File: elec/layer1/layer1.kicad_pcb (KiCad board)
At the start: 2 copper layers, 178 x 173.3 mm, 0 parts

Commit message: chore: l1 mux routing
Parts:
- added C1: 100nF, Capacitor_SMD:C_0603_1608Metric, F.Cu at (-14.4, 33.8)
- added C2: 100nF, Capacitor_SMD:C_0603_1608Metric, F.Cu at (-14.4, 36.3)
- added C3: 1000uF, Capacitor_THT:CP_Radial_D16.0mm_P7.50mm, F.Cu at (28.8, 127.8)
- added C4: 1000uF, Capacitor_THT:CP_Radial_D16.0mm_P7.50mm, F.Cu at (46.1, 127.3)
- added D1: LED, LED_SMD:LED_PLCC_2835, B.Cu at (109.6, 55.8)
- added D10: LED, LED_SMD:LED_PLCC_2835, B.Cu at (159.6, 116.7)
- added D11: LED, LED_SMD:LED_PLCC_2835, B.Cu at (156.7, 126.3)
- added D12: LED, LED_SMD:LED_PLCC_2835, B.Cu at (152.0, 135.1)
- added D13: LED, LED_SMD:LED_PLCC_2835, B.Cu at (145.7, 142.9)
- added D14: LED, LED_SMD:LED_PLCC_2835, B.Cu at (137.9, 149.2)
- added D15: LED, LED_SMD:LED_PLCC_2835, B.Cu at (129.1, 153.9)
- added D16: LED, LED_SMD:LED_PLCC_2835, B.Cu at (119.6, 156.8)
- added D17: LED, LED_SMD:LED_PLCC_2835, B.Cu at (109.6, 157.8)
- added D18: LED, LED_SMD:LED_PLCC_2835, B.Cu at (99.7, 156.8)
- added D19: LED, LED_SMD:LED_PLCC_2835, B.Cu at (90.1, 153.9)
- added D2: LED, LED_SMD:LED_PLCC_2835, B.Cu at (119.6, 56.8)
- added D20: LED, LED_SMD:LED_PLCC_2835, B.Cu at (81.3, 149.2)
- added D21: LED, LED_SMD:LED_PLCC_2835, B.Cu at (73.5, 142.9)
- added D22: LED, LED_SMD:LED_PLCC_2835, B.Cu at (67.2, 135.1)
- added D23: LED, LED_SMD:LED_PLCC_2835, B.Cu at (62.5, 126.3)
- added D24: LED, LED_SMD:LED_PLCC_2835, B.Cu at (59.6, 116.7)
- added D25: LED, LED_SMD:LED_PLCC_2835, B.Cu at (58.6, 106.8)
- added D26: LED, LED_SMD:LED_PLCC_2835, B.Cu at (59.6, 96.8)
- added D27: LED, LED_SMD:LED_PLCC_2835, B.Cu at (62.5, 87.3)
- added D28: LED, LED_SMD:LED_PLCC_2835, B.Cu at (67.2, 78.5)
- added D29: LED, LED_SMD:LED_PLCC_2835, B.Cu at (73.5, 70.7)
- added D3: LED, LED_SMD:LED_PLCC_2835, B.Cu at (129.1, 59.7)
- added D30: LED, LED_SMD:LED_PLCC_2835, B.Cu at (81.3, 64.4)
- added D31: LED, LED_SMD:LED_PLCC_2835, B.Cu at (90.1, 59.7)
- added D32: LED, LED_SMD:LED_PLCC_2835, B.Cu at (99.7, 56.8)
- added D33: D_Photo, Diode_SMD:D_0603_1608Metric, B.Cu at (104.6, 55.5)
- added D34: D_Photo, Diode_SMD:D_0603_1608Metric, B.Cu at (94.7, 57.5)
- added D35: D_Photo, Diode_SMD:D_0603_1608Metric, B.Cu at (85.3, 61.4)
- added D36: D_Photo, Diode_SMD:D_0603_1608Metric, B.Cu at (76.9, 67.0)
- added D37: D_Photo, Diode_SMD:D_0603_1608Metric, B.Cu at (69.8, 74.1)
- added D38: D_Photo, Diode_SMD:D_0603_1608Metric, B.Cu at (64.2, 82.5)
- added D39: D_Photo, Diode_SMD:D_0603_1608Metric, B.Cu at (60.3, 91.8)
- added D4: LED, LED_SMD:LED_PLCC_2835, B.Cu at (137.9, 64.4)
- added D40: D_Photo, Diode_SMD:D_0603_1608Metric, B.Cu at (58.4, 101.7)
- added D41: D_Photo, Diode_SMD:D_0603_1608Metric, B.Cu at (58.4, 111.8)
- added D42: D_Photo, Diode_SMD:D_0603_1608Metric, B.Cu at (60.3, 121.7)
- added D43: D_Photo, Diode_SMD:D_0603_1608Metric, B.Cu at (64.2, 131.1)
- added D44: D_Photo, Diode_SMD:D_0603_1608Metric, B.Cu at (69.8, 139.5)
- added D45: D_Photo, Diode_SMD:D_0603_1608Metric, B.Cu at (76.9, 146.6)
- added D46: D_Photo, Diode_SMD:D_0603_1608Metric, B.Cu at (85.3, 152.2)
- added D47: D_Photo, Diode_SMD:D_0603_1608Metric, B.Cu at (94.7, 156.1)
- added D48: D_Photo, Diode_SMD:D_0603_1608Metric, B.Cu at (104.6, 158.0)
- added D49: D_Photo, Diode_SMD:D_0603_1608Metric, B.Cu at (114.7, 158.0)
- added D5: LED, LED_SMD:LED_PLCC_2835, B.Cu at (145.7, 70.7)
- added D50: D_Photo, Diode_SMD:D_0603_1608Metric, B.Cu at (124.6, 156.1)
- added D51: D_Photo, Diode_SMD:D_0603_1608Metric, B.Cu at (133.9, 152.2)
- added D52: D_Photo, Diode_SMD:D_0603_1608Metric, B.Cu at (142.3, 146.6)
- added D53: D_Photo, Diode_SMD:D_0603_1608Metric, B.Cu at (149.4, 139.5)
- added D54: D_Photo, Diode_SMD:D_0603_1608Metric, B.Cu at (155.0, 131.1)
- added D55: D_Photo, Diode_SMD:D_0603_1608Metric, B.Cu at (158.9, 121.7)
- added D56: D_Photo, Diode_SMD:D_0603_1608Metric, B.Cu at (160.9, 111.8)
- added D57: D_Photo, Diode_SMD:D_0603_1608Metric, B.Cu at (160.9, 101.7)
- added D58: D_Photo, Diode_SMD:D_0603_1608Metric, B.Cu at (158.9, 91.8)
- added D59: D_Photo, Diode_SMD:D_0603_1608Metric, B.Cu at (155.0, 82.5)
- added D6: LED, LED_SMD:LED_PLCC_2835, B.Cu at (152.0, 78.5)
- added D60: D_Photo, Diode_SMD:D_0603_1608Metric, B.Cu at (149.4, 74.1)
- added D61: D_Photo, Diode_SMD:D_0603_1608Metric, B.Cu at (142.3, 67.0)
- added D62: D_Photo, Diode_SMD:D_0603_1608Metric, B.Cu at (133.9, 61.4)
- added D63: D_Photo, Diode_SMD:D_0603_1608Metric, B.Cu at (124.6, 57.5)
- added D64: D_Photo, Diode_SMD:D_0603_1608Metric, B.Cu at (114.7, 55.5)
- added D7: LED, LED_SMD:LED_PLCC_2835, B.Cu at (156.7, 87.3)
- added D8: LED, LED_SMD:LED_PLCC_2835, B.Cu at (159.6, 96.8)
- added D9: LED, LED_SMD:LED_PLCC_2835, B.Cu at (160.6, 106.8)
- added H1: MountingHole, MountingHole:MountingHole_2.2mm_M2_DIN965_Pad_TopBottom, F.Cu at (74.7, 31.5)
- added H10: MountingHole, MountingHole:MountingHole_3.2mm_M3_DIN965_Pad_TopBottom, F.Cu at (159.0, 77.2)
- added H11: MountingHole, MountingHole:MountingHole_3.2mm_M3_DIN965_Pad_TopBottom, F.Cu at (69.6, 84.3)
- added H12: MountingHole, MountingHole:MountingHole_3.2mm_M3_DIN965_Pad_TopBottom, F.Cu at (149.6, 84.3)
- added H13: MountingHole, MountingHole:MountingHole_3.2mm_M3_DIN965_Pad_TopBottom, F.Cu at (99.6, 84.9)
- added H14: MountingHole, MountingHole:MountingHole_3.2mm_M3_DIN965_Pad_TopBottom, F.Cu at (119.6, 84.9)
- added H15: MountingHole, MountingHole:MountingHole_3.2mm_M3_DIN965_Pad_TopBottom, F.Cu at (105.6, 96.8)
- added H16: MountingHole, MountingHole:MountingHole_3.2mm_M3_DIN965_Pad_TopBottom, F.Cu at (113.6, 96.8)
- added H17: MountingHole, MountingHole:MountingHole_3.2mm_M3_DIN965_Pad_TopBottom, F.Cu at (105.6, 116.8)
- added H18: MountingHole, MountingHole:MountingHole_3.2mm_M3_DIN965_Pad_TopBottom, F.Cu at (113.6, 116.8)
- added H19: MountingHole, MountingHole:MountingHole_3.2mm_M3_DIN965_Pad_TopBottom, F.Cu at (69.6, 129.3)
- added H2: MountingHole, MountingHole:MountingHole_2.2mm_M2_DIN965_Pad_TopBottom, F.Cu at (144.5, 31.5)
- added H20: MountingHole, MountingHole:MountingHole_3.2mm_M3_DIN965_Pad_TopBottom, F.Cu at (149.6, 129.3)
- added H21: MountingHole, MountingHole:MountingHole_3.2mm_M3_DIN965_Pad_TopBottom, F.Cu at (60.2, 136.4)
- added H22: MountingHole, MountingHole:MountingHole_3.2mm_M3_DIN965_Pad_TopBottom, F.Cu at (159.0, 136.4)
- added H23: MountingHole, MountingHole:MountingHole_3.2mm_M3_DIN965_Pad_TopBottom, F.Cu at (34.3, 141.7)
- added H24: MountingHole, MountingHole:MountingHole_3.2mm_M3_DIN965_Pad_TopBottom, F.Cu at (184.9, 141.7)
- added H25: MountingHole, MountingHole:MountingHole_3.2mm_M3_DIN965_Pad_TopBottom, F.Cu at (97.1, 147.2)
- added H26: MountingHole, MountingHole:MountingHole_3.2mm_M3_DIN965_Pad_TopBottom, F.Cu at (122.1, 147.2)
- added H27: MountingHole, MountingHole:MountingHole_3.2mm_M3_DIN965_Pad_TopBottom, F.Cu at (80.0, 156.2)
- added H28: MountingHole, MountingHole:MountingHole_3.2mm_M3_DIN965_Pad_TopBottom, F.Cu at (139.2, 156.2)
- added H29: MountingHole, MountingHole:MountingHole_3.2mm_M3_DIN965_Pad_TopBottom, F.Cu at (97.1, 172.2)
- added H3: MountingHole, MountingHole:MountingHole_3.2mm_M3_DIN965_Pad_TopBottom, F.Cu at (80.0, 57.4)
- added H30: MountingHole, MountingHole:MountingHole_3.2mm_M3_DIN965_Pad_TopBottom, F.Cu at (122.1, 172.2)
- added H31: MountingHole, MountingHole:MountingHole_3.2mm_M3_DIN965_Pad_TopBottom, F.Cu at (76.7, 183.0)
- added H32: MountingHole, MountingHole:MountingHole_3.2mm_M3_DIN965_Pad_TopBottom, F.Cu at (142.5, 183.0)
- added H33: MountingHole, MountingHole:MountingHole_2.2mm_M2_DIN965_Pad_TopBottom, F.Cu at (109.6, 142.2)
- added H34: MountingHole, MountingHole:MountingHole_2.2mm_M2_DIN965_Pad_TopBottom, F.Cu at (109.6, 172.2)
- added H4: MountingHole, MountingHole:MountingHole_3.2mm_M3_DIN965_Pad_TopBottom, F.Cu at (139.2, 57.4)
- added H5: MountingHole, MountingHole:MountingHole_3.2mm_M3_DIN965_Pad_TopBottom, F.Cu at (99.6, 64.9)
- added H6: MountingHole, MountingHole:MountingHole_3.2mm_M3_DIN965_Pad_TopBottom, F.Cu at (119.6, 64.9)
- added H7: MountingHole, MountingHole:MountingHole_3.2mm_M3_DIN965_Pad_TopBottom, F.Cu at (34.3, 71.9)
- added H8: MountingHole, MountingHole:MountingHole_3.2mm_M3_DIN965_Pad_TopBottom, F.Cu at (184.9, 71.9)
- added H9: MountingHole, MountingHole:MountingHole_3.2mm_M3_DIN965_Pad_TopBottom, F.Cu at (60.2, 77.2)
- added J1: XT30UPB-M, layer1-pcb-footprints:AMASS_XT30UPB-M, F.Cu at (-20.8, -16.2)
- added J2: XT30UPB-M, layer1-pcb-footprints:AMASS_XT30UPB-M, F.Cu at (-34.1, 7.05)
- added J3: Conn_01x04, Connector_JST:JST_XH_B4B-XH-AM_1x04_P2.50mm_Vertical, F.Cu at (84.2, 38.5)
- added J4: XT30UPB-M, layer1-pcb-footprints:AMASS_XT30UPB-M, F.Cu at (6.86, 77.5)
- added J5: XT30UPB-M, layer1-pcb-footprints:AMASS_XT30UPB-M, F.Cu at (48.1, 151.0)
- added R1: 10k, Capacitor_SMD:C_0603_1608Metric, F.Cu at (-14.4, 38.8)
- added R2: 3k, Capacitor_SMD:C_0603_1608Metric, F.Cu at (-14.4, 41.3)
- added R3: 3k, Capacitor_SMD:C_0603_1608Metric, F.Cu at (-14.4, 43.8)
- added R4: 10k, Capacitor_SMD:C_0603_1608Metric, F.Cu at (-14.4, 46.3)
- added SW2: SW_SPDT_312, layer1-pcb-footprints:SS12D00G3, F.Cu at (-36.5, 34.1)
- added TP1: TestPoint_2Pole, TestPoint:TestPoint_2Pads_Pitch2.54mm_Drill0.8mm, F.Cu at (-107.0, 48.6)
- added TP2: TestPoint_2Pole, TestPoint:TestPoint_2Pads_Pitch2.54mm_Drill0.8mm, F.Cu at (-107.0, 52.0)
- added TP3: TestPoint_2Pole, TestPoint:TestPoint_2Pads_Pitch2.54mm_Drill0.8mm, F.Cu at (-107.0, 55.4)
- added TP4: TestPoint_2Pole, TestPoint:TestPoint_2Pads_Pitch2.54mm_Drill0.8mm, F.Cu at (-107.0, 58.7)
- added TP5: TestPoint_2Pole, TestPoint:TestPoint_2Pads_Pitch2.54mm_Drill0.8mm, F.Cu at (-107.0, 62.0)
- added TP6: TestPoint_2Pole, TestPoint:TestPoint_2Pads_Pitch2.54mm_Drill0.8mm, F.Cu at (-107.0, 65.4)
- added TP7: TestPoint_2Pole, TestPoint:TestPoint_2Pads_Pitch2.54mm_Drill0.8mm, F.Cu at (-107.0, 68.8)
- added U1: CD74HC4067SM, layer1-pcb-footprints:CD74HC4067SM, B.Cu at (94.6, 106.8)
- added U2: CD74HC4067SM, layer1-pcb-footprints:CD74HC4067SM, B.Cu at (124.6, 106.8)
- added U3: TEENSY40, layer1-pcb-footprints:TEENSY40, F.Cu at (109.3, 34.6)
- added U4: ~, layer1-pcb-footprints:boost-module, F.Cu at (40.4, 98.0)
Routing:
- net Net-(D64-K): track 0.00 -> 50.4 mm
- net Net-(D48-K): track 0.00 -> 50.4 mm
- net Net-(D49-K): track 0.00 -> 50.4 mm
- net Net-(D33-K): track 0.00 -> 50.4 mm
- net Net-(D44-K): track 0.00 -> 49.7 mm
- net Net-(D53-K): track 0.00 -> 49.6 mm
- net Net-(D50-K): track 0.00 -> 47.0 mm
- net Net-(D47-K): track 0.00 -> 47.0 mm
- net Net-(D45-K): track 0.00 -> 46.6 mm
- net Net-(D52-K): track 0.00 -> 46.5 mm
- net Net-(D63-K): track 0.00 -> 45.3 mm
- net Net-(D34-K): track 0.00 -> 45.3 mm
- net Net-(D62-K): track 0.00 -> 45.0 mm
- net Net-(D51-K): track 0.00 -> 45.0 mm
- net Net-(D46-K): track 0.00 -> 45.0 mm
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- added copper zone on B.Cu, net GND
- added copper zone on F.Cu, net GND
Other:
- outline, holes or cut-outs redrawn

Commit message: feat: complete layer1
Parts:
- added TP8: TestPoint_2Pole, TestPoint:TestPoint_2Pads_Pitch2.54mm_Drill0.8mm, F.Cu at (191.9, 111.5)
- C1, C2, R1, R2, R3, R4: moved to B.Cu
- J1, J2, J4, J5: value XT30UPB-M -> XT30PW-M; footprint layer1-pcb-footprints:AMASS_XT30UPB-M -> layer1-pcb-footprints:AMASS_XT30PW-M
- moved TP3 305.4 mm to (191.9, 118.0), turned to 90 degrees
- moved TP2 303.5 mm to (191.9, 105.0), turned to 90 degrees
- moved TP1 303.0 mm to (191.9, 98.5), turned to 90 degrees
- moved TP4 239.6 mm to (129.9, 22.3), turned to -90 degrees
- moved TP6 239.5 mm to (129.9, 30.0), turned to 90 degrees
- moved TP7 239.2 mm to (129.9, 35.3), turned to 90 degrees
- moved TP5 237.8 mm to (129.9, 40.5), turned to 90 degrees
- moved J1 231.1 mm to (184.6, 89.8), turned to 180 degrees
- moved J2 219.9 mm to (169.6, 89.8), turned to 180 degrees
- moved J4 169.2 mm to (169.6, 123.8)
- moved C1 160.5 mm to (129.9, 104.0), turned to -90 degrees
- moved R3 158.5 mm to (129.9, 109.5), turned to 90 degrees
- moved R4 146.6 mm to (121.9, 100.3), turned to 90 degrees
- moved J5 139.2 mm to (184.6, 123.8)
- moved R1 134.5 mm to (98.1, 112.5)
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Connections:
- J4 pad P: +12V -> +24V
- J5 pad P: +24V -> +12V
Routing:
- net +3V3: track 0.00 -> 242.8 mm, vias 0 -> 2
- net +12V: track 0.00 -> 203.2 mm
- net +24V: track 0.00 -> 174.1 mm
- net /Mux Com (0-15): track 0.00 -> 148.1 mm, vias 0 -> 1
- net /S0: track 0.00 -> 145.1 mm, vias 0 -> 1
- net /S1: track 0.00 -> 144.8 mm, vias 0 -> 3
- net /S2: track 0.00 -> 144.6 mm, vias 0 -> 3
- net /S3: track 0.00 -> 138.7 mm, vias 0 -> 4
- net +5V: track 0.00 -> 133.5 mm
- net /Mux Com (16-31): track 0.00 -> 109.3 mm, vias 0 -> 1
- net /RX (L1-Teensy): track 0.00 -> 64.5 mm
- net /TX (L1-Teensy): track 0.00 -> 58.2 mm
- net 3v3 - LED, Photodiode: track 0.00 -> 36.8 mm
- net Net-(U2-~{E}): track 0.00 -> 2.45 mm
- net Net-(U1-~{E}): track 0.00 -> 2.43 mm
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- added copper zone on F.Cu, net +12V
- added copper zone on F.Cu, net +24V
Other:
- outline, holes or cut-outs redrawn
- board text added: "12v"
- board text added: "24v"
- board text added: "3v3"
- board text added: "5v"
- board text added: "L2"
- board text added: "MUX 00-15"
- board text added: "MUX 16-31"
- board text added: "RX"
- board text added: "S0"
- board text added: "S1"
- board text added: "S2"
- board text added: "S3"
- board text added: "SW"
- board text added: "TX"
- board text added: "Vent Exhaust"

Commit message: fix: l1 gnd
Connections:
- U3 pad G1: unconnected-(U3-PadG1) -> GND
- U3 pad G2: unconnected-(U3-PadG2) -> GND
- U3 pad G3: unconnected-(U3-PadG3) -> GND

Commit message: fix: l1; chore: l2 schematics
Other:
- outline, holes or cut-outs redrawn

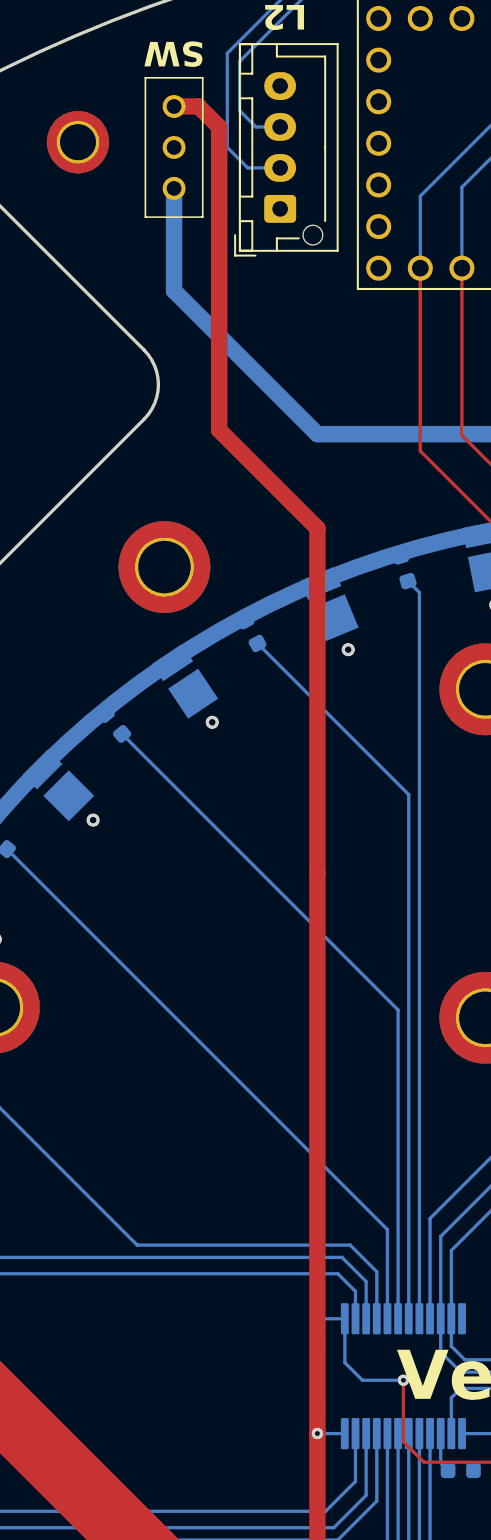
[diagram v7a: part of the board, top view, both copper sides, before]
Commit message: changed chenxuan mistake on l1
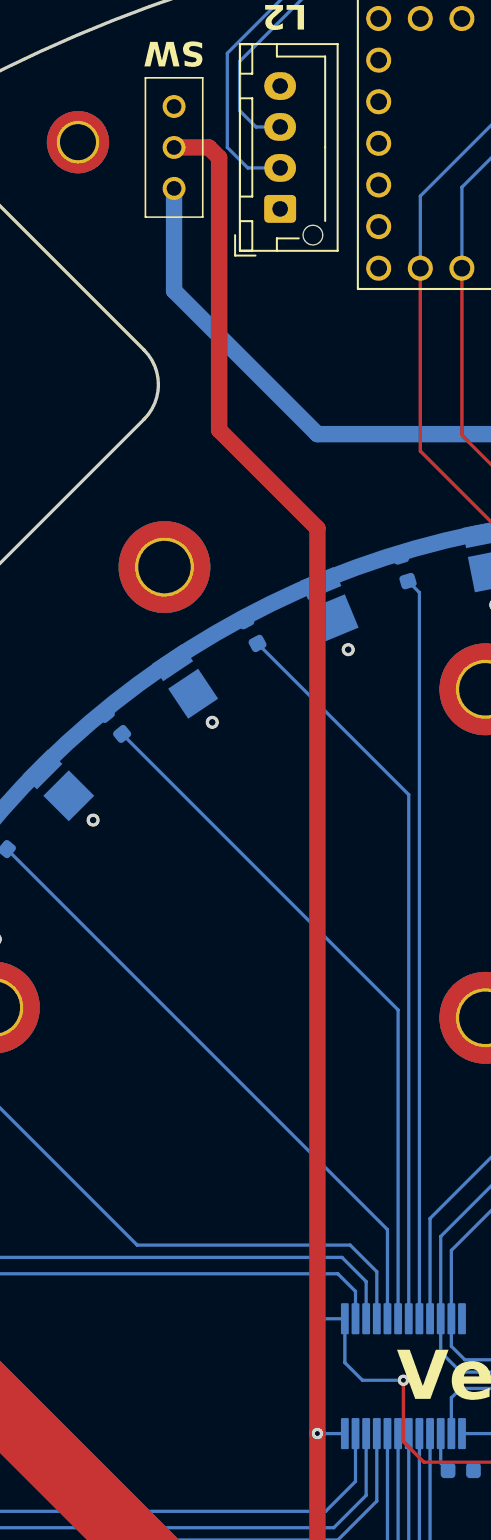
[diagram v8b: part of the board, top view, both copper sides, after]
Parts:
- turned SW2 to -90 degrees
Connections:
- SW2 pad 1: 3v3 - LED, Photodiode -> GND
- SW2 pad 2: GND -> +3V3
- SW2 pad 3: +3V3 -> 3v3 - LED, Photodiode
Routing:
- net +3V3: track 242.8 -> 240.7 mm
